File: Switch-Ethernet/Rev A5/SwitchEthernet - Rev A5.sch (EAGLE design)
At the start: 118 parts, among them J1 22-05-7028-02, J2 NE8FAV, J3 NE8FAV, J4 DF17(4.0)-20DS-0.5V(57), J5 DF17(4.0)-20DP-0.5V(57), J6 RB1-125BAG1A, T1 H1102FNL, T2 H1102FNL, T3 EXMACHINA-LOGO-NAME, U1 TC1264-3.3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

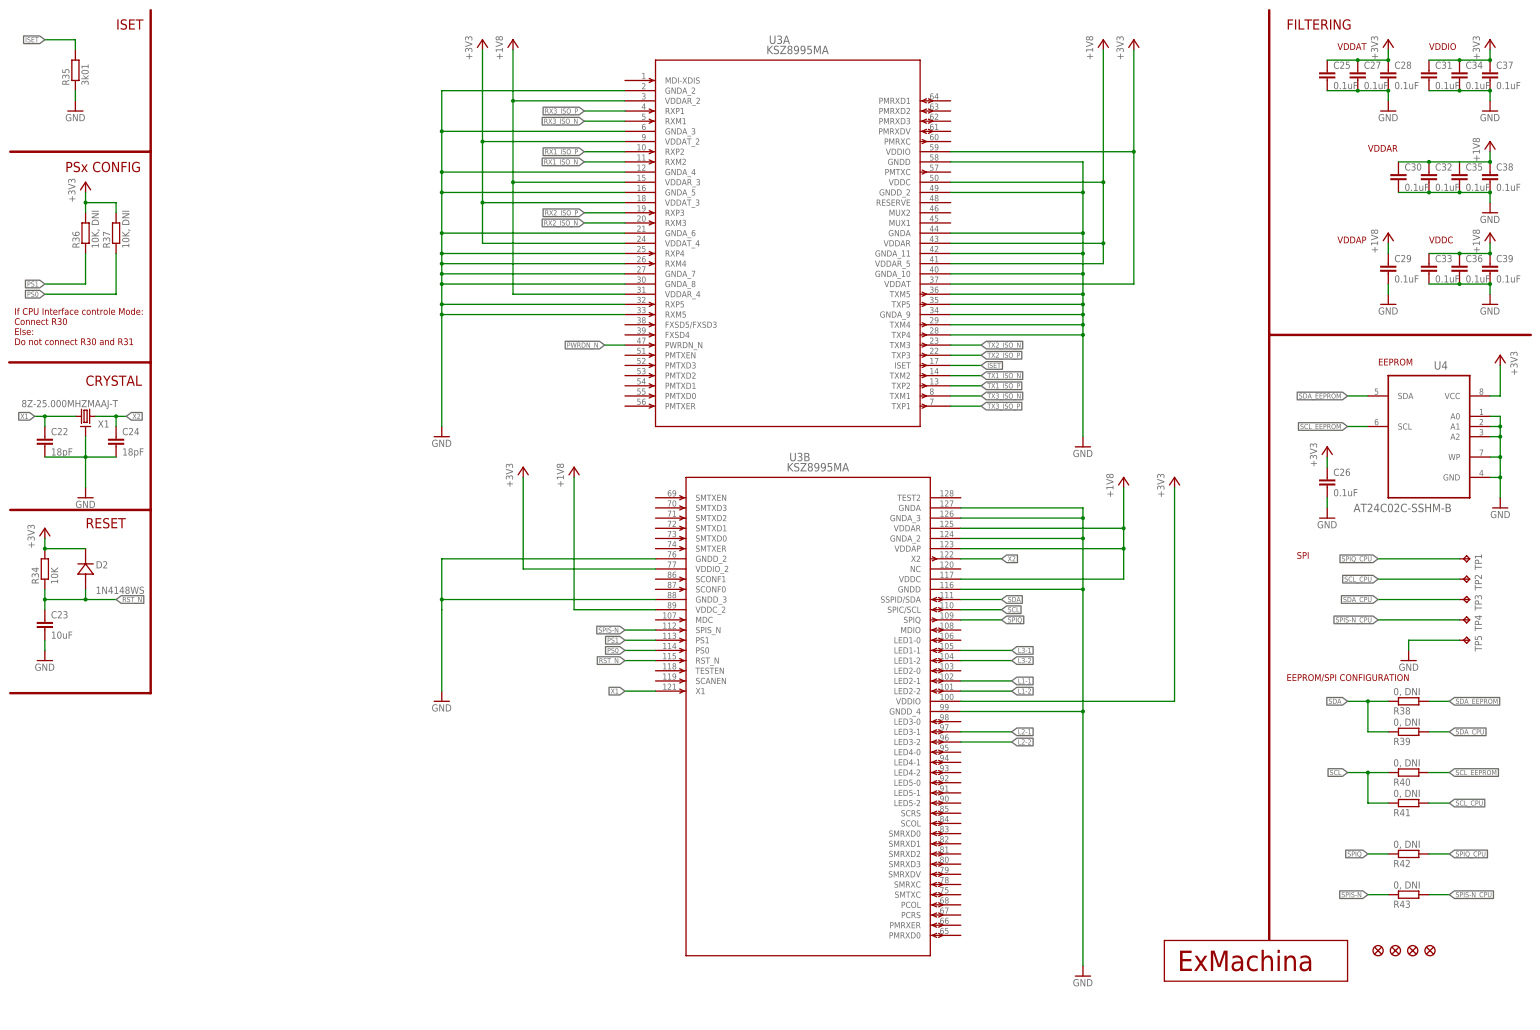
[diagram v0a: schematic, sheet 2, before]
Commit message: Reorganization of schematic layouts
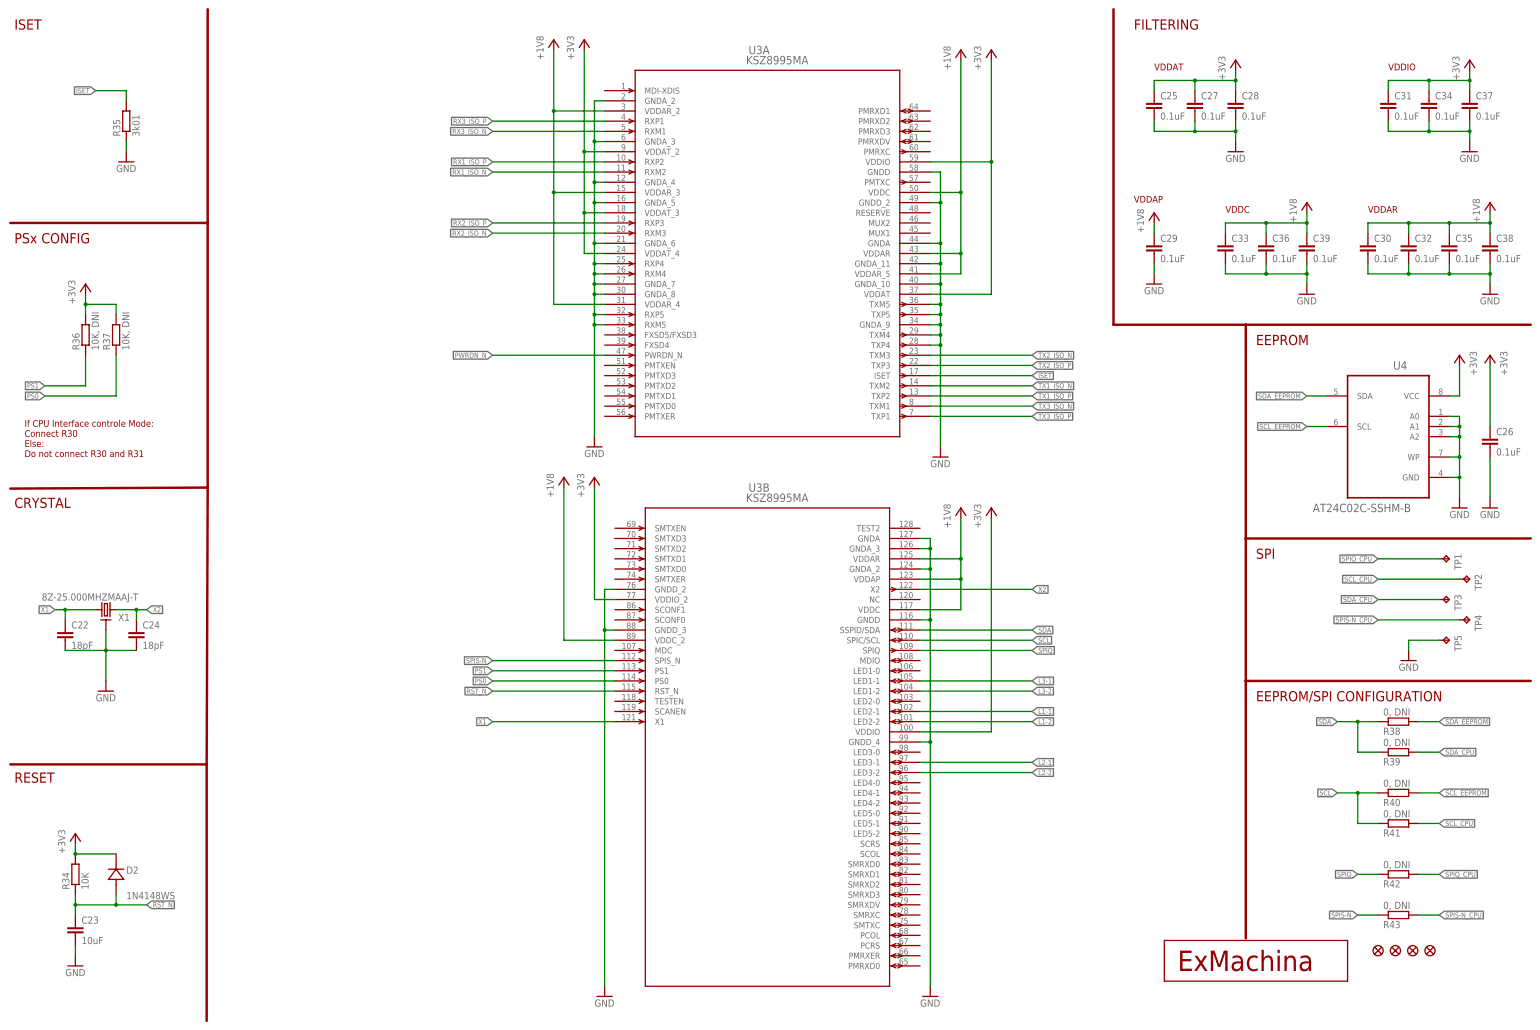
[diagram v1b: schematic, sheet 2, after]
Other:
- note added: "Board to board connection"
- note added: "ETHERNET 1"
- note added: "ETHERNET 2"
- moved on the sheet: C1, C13, C14, C15, C16, C17, C18, C2, C22, C23, C24, C25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
